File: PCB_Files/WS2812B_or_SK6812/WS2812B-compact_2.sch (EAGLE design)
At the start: 41 parts, among them P1 HT7333

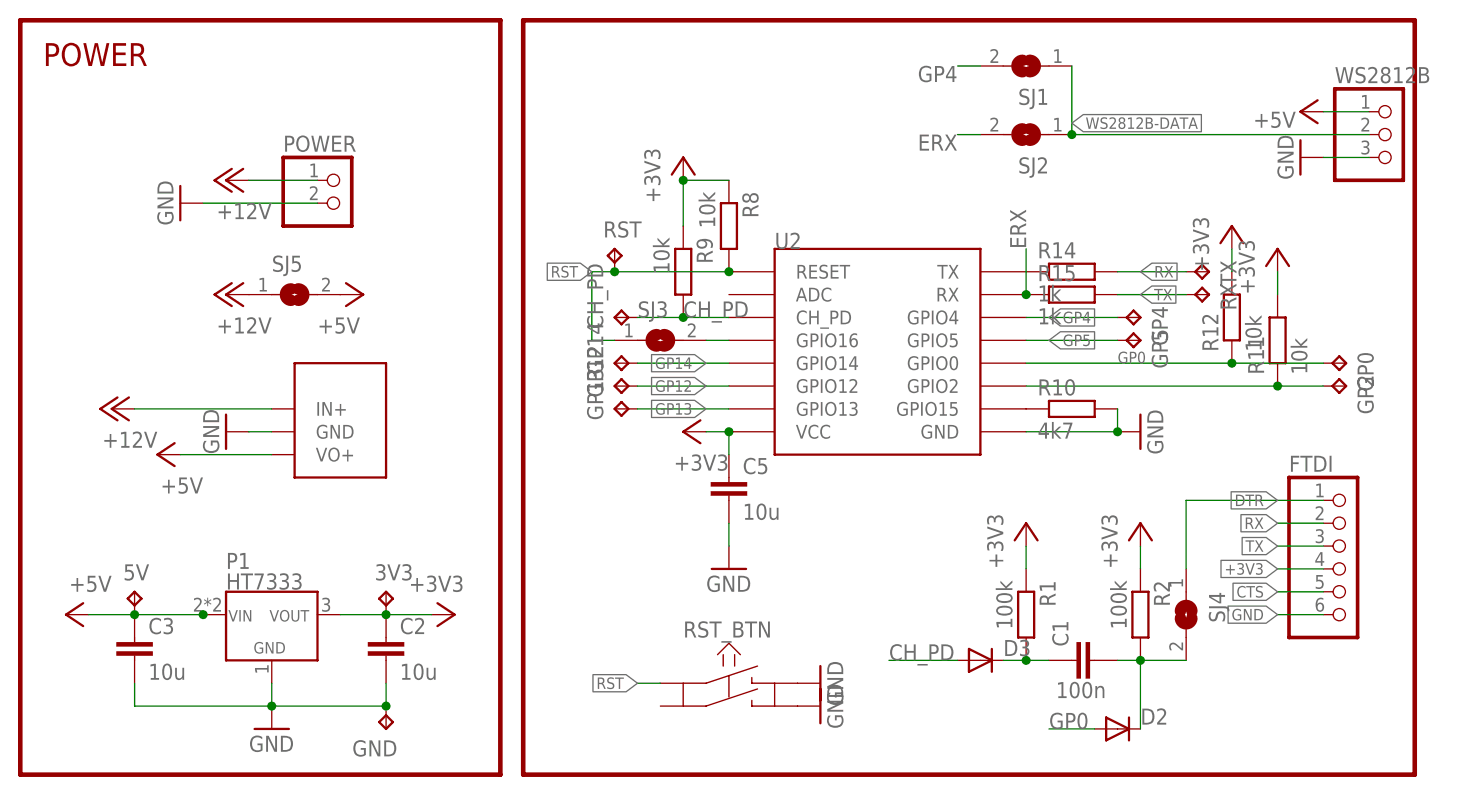
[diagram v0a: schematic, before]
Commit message: created additional compact design of ws2812b module
this new design features smaller footprint, but the esp module ist partially outside the board, which will result in better wifi connection.

additionally the footprint of the HT7333 has been fixed as previously it had used the wrong package.
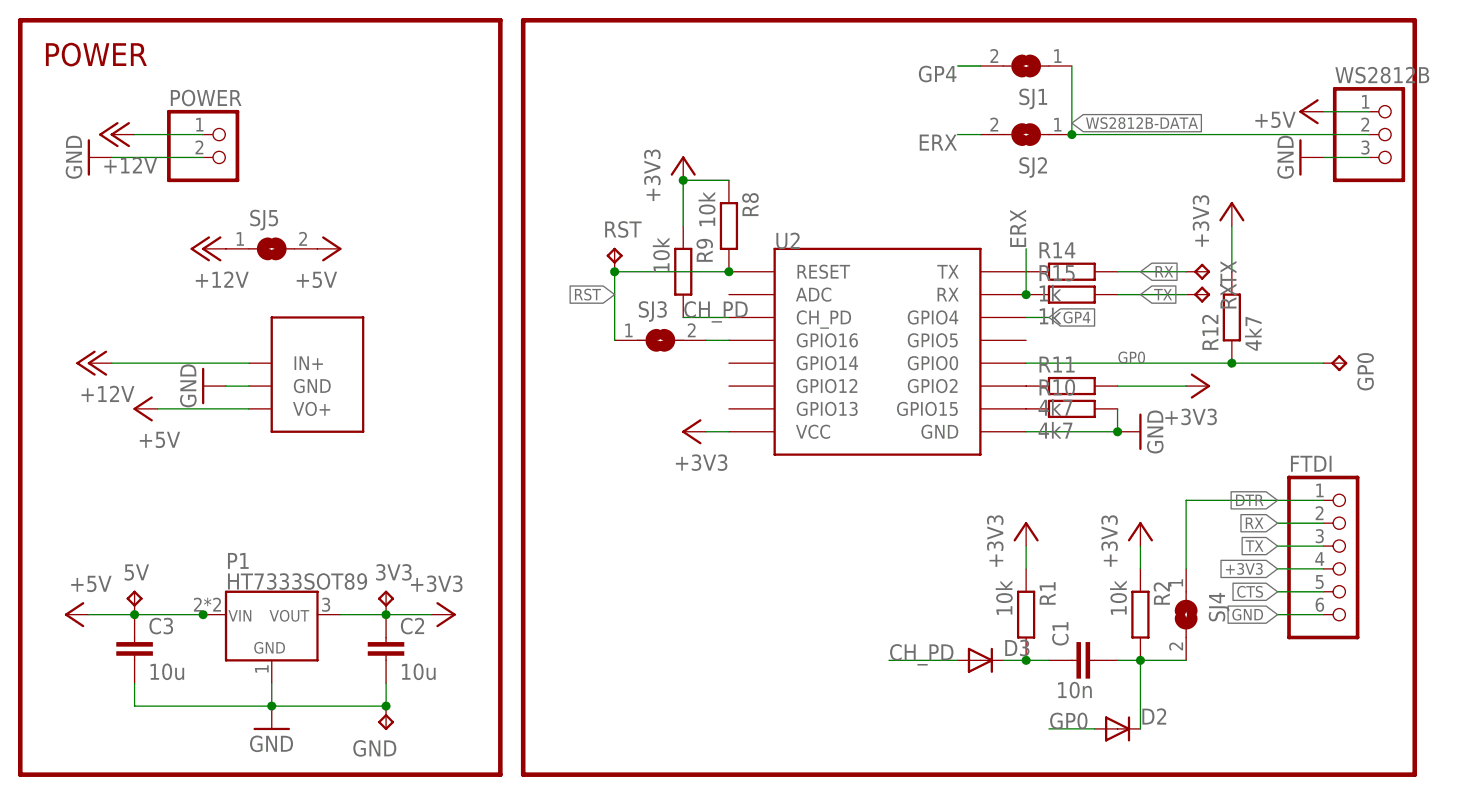
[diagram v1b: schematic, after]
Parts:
- removed C5: 10u, rcl:C-EUC1206
- removed CH_PD, GP12, GP13, GP14, GP2, GP4, GP5: TPB1,27, testpad:TPB1,27
- removed RST_BTN: (no value), schalter_taster:KSM611A
- 3V3, 5V, GND: value TPB2,54 -> TPB1,27; device testpad:TPB2,54 -> testpad:TPB1,27
- C1: value 100n -> 10n; device rcl:C-EUC1206 -> rcl:C-EUC0805
- C2, C3: device rcl:C-EUC1206 -> rcl:C-EUC0805
- P1: value HT7333 -> HT7333SOT89
- R1, R2: value 100k -> 10k
- R11, R12: value 10k -> 4k7
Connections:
- removed net GP12: GP12.TP, U2.GPIO12
- removed net GP13: GP13.TP, U2.GPIO13
- removed net GP14: GP14.TP, U2.GPIO14
- removed net GP5: GP5.TP, U2.GPIO5
- net +3V3: no longer C5.1
- net CH_PD: no longer CH_PD.TP
- net GND: no longer C5.2, RST_BTN.B, RST_BTN.D
- net GP4: no longer GP4.TP
- net N$5: no longer GP2.TP
- net RST: no longer RST_BTN.A
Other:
- moved on the sheet: POWER, R11, SJ5
